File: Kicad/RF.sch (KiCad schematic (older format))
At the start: 2 parts, among them P1 nRF24l01

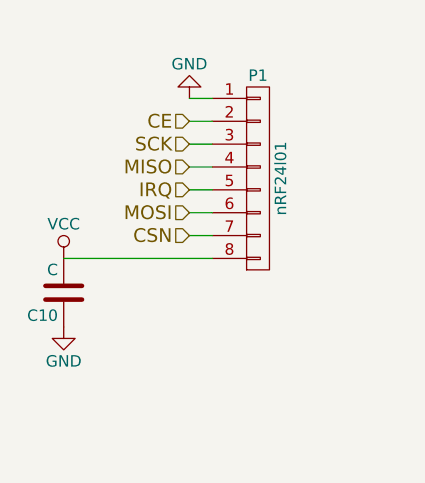
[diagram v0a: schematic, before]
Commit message: Se inició con el Pcb. Se eliminó el capacitor del socket del nrf. Se cambió el conector de la bat.
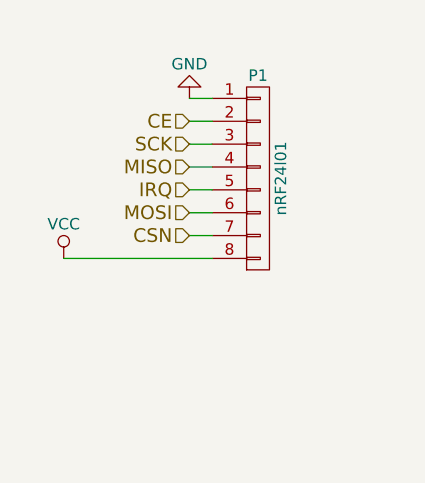
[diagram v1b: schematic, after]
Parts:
- removed C10: C, EMG:C_0805, symbol C
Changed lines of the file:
@@
 Wire Wire Line
 	4850 3600 4950 3600
-$Comp
-L C C10
-U 1 1 57FAB4AD
-P 4300 3850
-F 0 "C10" H 4325 3950 50  0000 L CNN
-F 1 "C" H 4325 3750 50  0000 L CNN
-F 2 "EMG:C_0805" H 4338 3700 50  0001 C CNN
-F 3 "" H 4300 3850 50  0000 C CNN
-	1    4300 3850
-	-1   0    0    1
-$EndComp
-$Comp
-L GND #PWR015
-U 1 1 57FAB5CE
-P 4300 4000
-F 0 "#PWR015" H 4300 3750 50  0001 C CNN
-F 1 "GND" H 4300 3850 50  0000 C CNN
-F 2 "" H 4300 4000 50  0000 C CNN
-F 3 "" H 4300 4000 50  0000 C CNN
-	1    4300 4000
-	1    0    0    -1
-$EndComp
 Wire Wire Line
 	4950 3700 4300 3700

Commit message: Se incluyó nuevamente el C12.
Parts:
- added C12: C, EMG:C_0805, symbol C
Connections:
- net GND: now also C12.2
- net VCC: now also C12.1
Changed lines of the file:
@@
 Wire Wire Line
 	4950 3700 4300 3700
+$Comp
+L C C12
+U 1 1 58C15947
+P 4850 4100
+F 0 "C12" H 4875 4200 50  0000 L CNN
+F 1 "C" H 4875 4000 50  0000 L CNN
+F 2 "EMG:C_0805" H 4888 3950 50  0001 C CNN
+F 3 "" H 4850 4100 50  0000 C CNN
+	1    4850 4100
+	1    0    0    -1
+$EndComp
+Wire Wire Line
+	4850 3950 4850 3700
+Connection ~ 4850 3700
+$Comp
+L GND #PWR015
+U 1 1 58C159A2
+P 4850 4400
+F 0 "#PWR015" H 4850 4150 50  0001 C CNN
+F 1 "GND" H 4850 4250 50  0000 C CNN
+F 2 "" H 4850 4400 50  0000 C CNN
+F 3 "" H 4850 4400 50  0000 C CNN
+	1    4850 4400
+	1    0    0    -1
+$EndComp
+Wire Wire Line
+	4850 4250 4850 4400
 $EndSCHEMATC

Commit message: Versión unificada
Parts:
- C12: footprint EMG:C_0805 -> EMG:C_0603
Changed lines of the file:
@@
 F 0 "C12" H 4875 4200 50  0000 L CNN
 F 1 "C" H 4875 4000 50  0000 L CNN
-F 2 "EMG:C_0805" H 4888 3950 50  0001 C CNN
+F 2 "EMG:C_0603" H 4888 3950 50  0001 C CNN
 F 3 "" H 4850 4100 50  0000 C CNN
 	1    4850 4100

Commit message: Ruteo pcb
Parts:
- P1: footprint EMG:Pin_Header_Straight_1x08_Pitch1.27mm -> EMG:nRF
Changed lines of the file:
@@
 F 0 "P1" H 5150 3800 50  0000 C CNN
 F 1 "nRF24l01" V 5250 3350 50  0000 C CNN
-F 2 "EMG:Pin_Header_Straight_1x08_Pitch1.27mm" H 5150 3350 50  0001 C CNN
+F 2 "EMG:nRF" H 5150 3350 50  0001 C CNN
 F 3 "" H 5150 3350 50  0000 C CNN
 	1    5150 3350

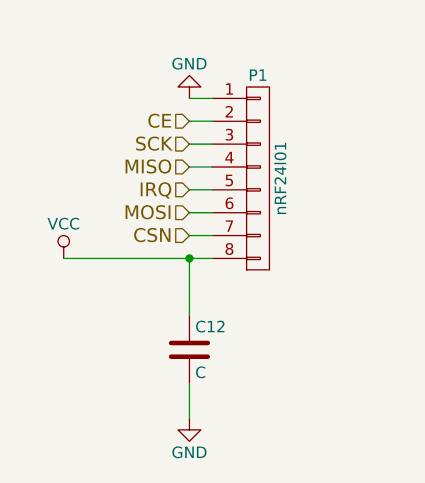
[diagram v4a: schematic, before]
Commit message: Se cambió el pin out de nRF en el esquemático y se hicieron las nuevas conexiones en el pcb.
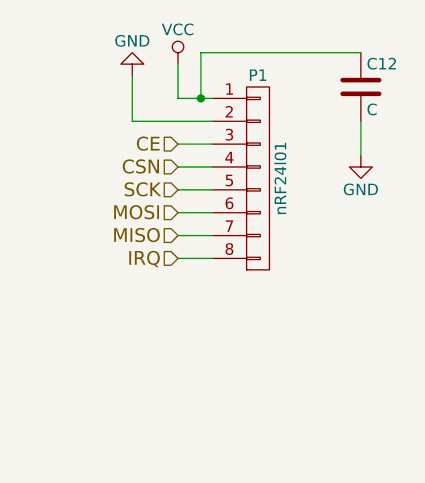
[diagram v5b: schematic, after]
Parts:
- P1: footprint EMG:nRF -> EMG:nRF2
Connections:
- net CE: now also P1.3 (P3); no longer P1.2 (P2)
- net CSN: now also P1.4 (P4); no longer P1.7 (P7)
- net GND: now also P1.2 (P2); no longer P1.1 (P1)
- net IRQ: now also P1.8 (P8); no longer P1.5 (P5)
- net MISO: now also P1.7 (P7); no longer P1.4 (P4)
- net SCK: now also P1.5 (P5); no longer P1.3 (P3)
- net VCC: now also P1.1 (P1); no longer P1.8 (P8)
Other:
- moved on the sheet: C12
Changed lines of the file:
@@
 F 0 "P1" H 5150 3800 50  0000 C CNN
 F 1 "nRF24l01" V 5250 3350 50  0000 C CNN
-F 2 "EMG:nRF" H 5150 3350 50  0001 C CNN
+F 2 "EMG:nRF2" H 5150 3350 50  0001 C CNN
 F 3 "" H 5150 3350 50  0000 C CNN
 	1    5150 3350
@@
 L GND #PWR013
 U 1 1 57DD9164
-P 4850 3000
-F 0 "#PWR013" H 4850 2750 50  0001 C CNN
-F 1 "GND" H 4850 2850 50  0000 C CNN
-F 2 "" H 4850 3000 50  0000 C CNN
-F 3 "" H 4850 3000 50  0000 C CNN
-	1    4850 3000
+P 4600 2900
+F 0 "#PWR013" H 4600 2650 50  0001 C CNN
+F 1 "GND" H 4600 2750 50  0000 C CNN
+F 2 "" H 4600 2900 50  0000 C CNN
+F 3 "" H 4600 2900 50  0000 C CNN
+	1    4600 2900
 	-1   0    0    1
 $EndComp
@@
 L VCC #PWR014
 U 1 1 57DD917A
-P 4300 3700
-F 0 "#PWR014" H 4300 3550 50  0001 C CNN
-F 1 "VCC" H 4300 3850 50  0000 C CNN
-F 2 "" H 4300 3700 50  0000 C CNN
-F 3 "" H 4300 3700 50  0000 C CNN
-	1    4300 3700
+P 4800 2850
+F 0 "#PWR014" H 4800 2700 50  0001 C CNN
+F 1 "VCC" H 4800 3000 50  0000 C CNN
+F 2 "" H 4800 2850 50  0000 C CNN
+F 3 "" H 4800 2850 50  0000 C CNN
+	1    4800 2850
 	1    0    0    -1
 $EndComp
-Text HLabel 4850 3100 0    60   Input ~ 0
+Text HLabel 4800 3200 0    60   Input ~ 0
 CE
-Text HLabel 4850 3200 0    60   Input ~ 0
+Text HLabel 4800 3400 0    60   Input ~ 0
 SCK
-Text HLabel 4850 3300 0    60   Input ~ 0
+Text HLabel 4800 3600 0    60   Input ~ 0
 MISO
-Text HLabel 4850 3400 0    60   Input ~ 0
+Text HLabel 4800 3700 0    60   Input ~ 0
 IRQ
-Text HLabel 4850 3500 0    60   Input ~ 0
+Text HLabel 4800 3500 0    60   Input ~ 0
 MOSI
-Text HLabel 4850 3600 0    60   Input ~ 0
+Text HLabel 4800 3300 0    60   Input ~ 0
 CSN
 Wire Wire Line
-	4850 3000 4950 3000
-Wire Wire Line
-	4850 3100 4950 3100
-Wire Wire Line
-	4850 3200 4950 3200
-Wire Wire Line
-	4850 3300 4950 3300
-Wire Wire Line
-	4850 3400 4950 3400
-Wire Wire Line
-	4850 3500 4950 3500
-Wire Wire Line
-	4850 3600 4950 3600
-Wire Wire Line
-	4950 3700 4300 3700
+	4600 3100 4950 3100
 $Comp
 L C C12
 U 1 1 58C15947
-P 4850 4100
-F 0 "C12" H 4875 4200 50  0000 L CNN
-F 1 "C" H 4875 4000 50  0000 L CNN
-F 2 "EMG:C_0603" H 4888 3950 50  0001 C CNN
-F 3 "" H 4850 4100 50  0000 C CNN
-	1    4850 4100
+P 5600 2950
+F 0 "C12" H 5625 3050 50  0000 L CNN
+F 1 "C" H 5625 2850 50  0000 L CNN
+F 2 "EMG:C_0603" H 5638 2800 50  0001 C CNN
+F 3 "" H 5600 2950 50  0000 C CNN
+	1    5600 2950
+	1    0    0    -1
+$EndComp
+$Comp
+L GND #PWR015
+U 1 1 58C159A2
+P 5600 3250
+F 0 "#PWR015" H 5600 3000 50  0001 C CNN
+F 1 "GND" H 5600 3100 50  0000 C CNN
+F 2 "" H 5600 3250 50  0000 C CNN
+F 3 "" H 5600 3250 50  0000 C CNN
+	1    5600 3250
 	1    0    0    -1
 $EndComp
 Wire Wire Line
-	4850 3950 4850 3700
-Connection ~ 4850 3700
-$Comp
-L GND #PWR015
-U 1 1 58C159A2
-P 4850 4400
-F 0 "#PWR015" H 4850 4150 50  0001 C CNN
-F 1 "GND" H 4850 4250 50  0000 C CNN
-F 2 "" H 4850 4400 50  0000 C CNN
-F 3 "" H 4850 4400 50  0000 C CNN
-	1    4850 4400
-	1    0    0    -1
-$EndComp
+	5600 3100 5600 3250
 Wire Wire Line
-	4850 4250 4850 4400
+	4950 3000 4800 3000
+Wire Wire Line
+	4800 3000 4800 2850
+Wire Wire Line
+	4600 3100 4600 2900
+Wire Wire Line
+	4800 3200 4950 3200
+Wire Wire Line
+	4800 3300 4950 3300
+Wire Wire Line
+	4800 3400 4950 3400
+Wire Wire Line
+	4800 3500 4950 3500
+Wire Wire Line
+	4800 3600 4950 3600
+Wire Wire Line
+	4800 3700 4950 3700
+Wire Wire Line
+	5600 2800 4900 2800
+Wire Wire Line
+	4900 2800 4900 3000
+Connection ~ 4900 3000
 $EndSCHEMATC

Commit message: Se cambió la huella del nrf.
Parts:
- P1: footprint EMG:nRF2 -> EMG:nRF
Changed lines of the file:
@@
 F 0 "P1" H 5150 3800 50  0000 C CNN
 F 1 "nRF24l01" V 5250 3350 50  0000 C CNN
-F 2 "EMG:nRF2" H 5150 3350 50  0001 C CNN
+F 2 "EMG:nRF" H 5150 3350 50  0001 C CNN
 F 3 "" H 5150 3350 50  0000 C CNN
 	1    5150 3350
